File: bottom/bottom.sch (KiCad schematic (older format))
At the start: 1 part

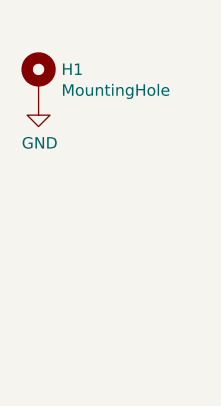
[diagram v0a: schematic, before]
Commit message: add mounting holes to sch
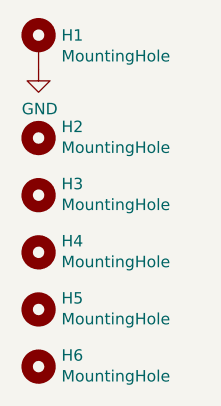
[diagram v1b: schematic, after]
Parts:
- added H2, H3, H4, H5, H6: MountingHole, MountingHole:MountingHole_2.2mm_M2_Pad, symbol Mechanical:MountingHole
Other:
- moved on the sheet: H1
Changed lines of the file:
@@
 L Mechanical:MountingHole_Pad H1
 U 1 1 61D3B113
-P 3450 3350
-F 0 "H1" H 3550 3399 50  0000 L CNN
-F 1 "MountingHole" H 3550 3308 50  0000 L CNN
-F 2 "MountingHole:MountingHole_2.2mm_M2_Pad" H 3450 3350 50  0001 C CNN
-F 3 "~" H 3450 3350 50  0001 C CNN
-	1    3450 3350
+P 3450 3200
+F 0 "H1" H 3550 3249 50  0000 L CNN
+F 1 "MountingHole" H 3550 3158 50  0000 L CNN
+F 2 "MountingHole:MountingHole_2.2mm_M2_Pad" H 3450 3200 50  0001 C CNN
+F 3 "~" H 3450 3200 50  0001 C CNN
+	1    3450 3200
 	1    0    0    -1
 $EndComp
 $Comp
-L power:GND #PWR0101
-U 1 1 61D3D7CD
-P 3450 3450
-F 0 "#PWR0101" H 3450 3200 50  0001 C CNN
-F 1 "GND" H 3455 3277 50  0000 C CNN
-F 2 "" H 3450 3450 50  0001 C CNN
-F 3 "" H 3450 3450 50  0001 C CNN
-	1    3450 3450
+L Mechanical:MountingHole H2
+U 1 1 61D7D108
+P 3450 3600
+F 0 "H2" H 3550 3649 50  0000 L CNN
+F 1 "MountingHole" H 3550 3558 50  0000 L CNN
+F 2 "MountingHole:MountingHole_2.2mm_M2_Pad" H 3450 3600 50  0001 C CNN
+F 3 "~" H 3450 3600 50  0001 C CNN
+	1    3450 3600
 	1    0    0    -1
 $EndComp
+$Comp
+L Mechanical:MountingHole H3
+U 1 1 61D7D3F6
+P 3450 3850
+F 0 "H3" H 3550 3899 50  0000 L CNN
+F 1 "MountingHole" H 3550 3808 50  0000 L CNN
+F 2 "MountingHole:MountingHole_2.2mm_M2_Pad" H 3450 3850 50  0001 C CNN
+F 3 "~" H 3450 3850 50  0001 C CNN
+	1    3450 3850
+	1    0    0    -1
+$EndComp
+$Comp
+L Mechanical:MountingHole H4
+U 1 1 61D7D6ED
+P 3450 4100
+F 0 "H4" H 3550 4149 50  0000 L CNN
+F 1 "MountingHole" H 3550 4058 50  0000 L CNN
+F 2 "MountingHole:MountingHole_2.2mm_M2_Pad" H 3450 4100 50  0001 C CNN
+F 3 "~" H 3450 4100 50  0001 C CNN
+	1    3450 4100
+	1    0    0    -1
+$EndComp
+$Comp
+L Mechanical:MountingHole H5
+U 1 1 61D7D97E
+P 3450 4350
+F 0 "H5" H 3550 4399 50  0000 L CNN
+F 1 "MountingHole" H 3550 4308 50  0000 L CNN
+F 2 "MountingHole:MountingHole_2.2mm_M2_Pad" H 3450 4350 50  0001 C CNN
+F 3 "~" H 3450 4350 50  0001 C CNN
+	1    3450 4350
+	1    0    0    -1
+$EndComp
+$Comp
+L Mechanical:MountingHole H6
+U 1 1 61D7DC06
+P 3450 4600
+F 0 "H6" H 3550 4649 50  0000 L CNN
+F 1 "MountingHole" H 3550 4558 50  0000 L CNN
+F 2 "MountingHole:MountingHole_2.2mm_M2_Pad" H 3450 4600 50  0001 C CNN
+F 3 "~" H 3450 4600 50  0001 C CNN
+	1    3450 4600
+	1    0    0    -1
+$EndComp
+$Comp
+L power:GND #PWR?
+U 1 1 61D7E46C
+P 3450 3300
+F 0 "#PWR?" H 3450 3050 50  0001 C CNN
+F 1 "GND" H 3455 3127 50  0000 C CNN
+F 2 "" H 3450 3300 50  0001 C CNN
+F 3 "" H 3450 3300 50  0001 C CNN
+	1    3450 3300
+	1    0    0    -1
+$EndComp
